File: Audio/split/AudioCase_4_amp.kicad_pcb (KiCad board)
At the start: 2 copper layers, 61.6 x 41.5 mm, 26 parts, among them J10 AMP_AUX_IN, J11 AMP_AUX_OUT, J9 AMP_PWR

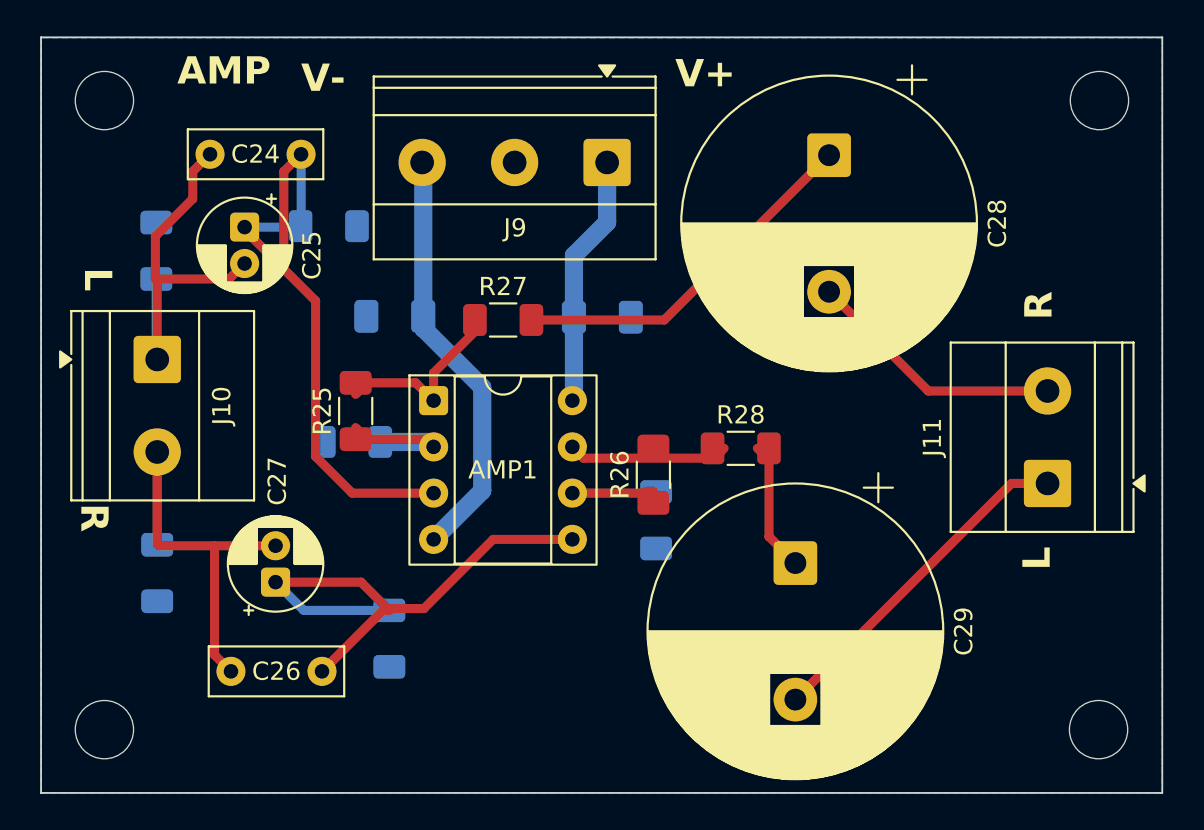
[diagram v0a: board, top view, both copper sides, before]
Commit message: ノイズ対策と製造データ整備: デカップリング追加・GNDベタ強化・シルク整理
- 5V_+ラインにデカップリング/バルク(C34-C37)を追加し、リレー切替時の電源変動を抑制
- F.CuにCTRL_GND/GNDベタを追加し、ステッチングビアで表裏GNDを補強(DC-DC周辺含む)
- 端子台ラベル等のシルク重なりを解消(J11/J14/J6/J4/L1/L2ほか)
- masterから4基板を再split、Gerber/zipを再生成

Co-authored-by: Cursor <cursoragent@cursor.com>
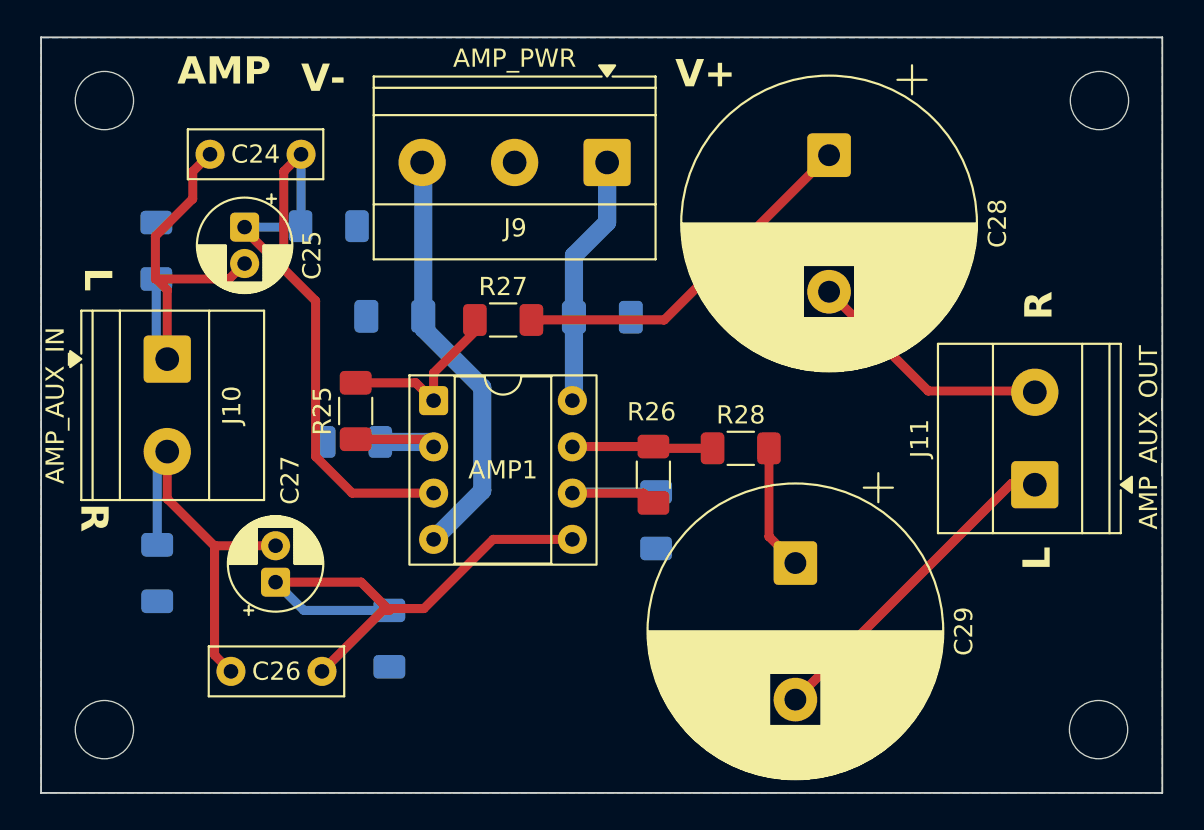
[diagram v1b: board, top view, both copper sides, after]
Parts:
- moved J11 0.70 mm to (172.3, 44.6)
- moved J10 0.55 mm to (124.6, 37.7)
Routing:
- net /Controll/L_OUT: track 24.0 -> 22.3 mm
- net Net-(AMP1-Pad7): track 8.82 -> 7.75 mm
- net Net-(AMP1A--): track 7.76 -> 6.86 mm
- net /Controll/R_OUT: track 22.2 -> 23.0 mm
- net /AmpModule/R_OUT: track 14.3 -> 13.6 mm
- net /AmpModule/L_OUT: track 18.8 -> 18.1 mm

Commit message: AudioCaseのリレー・EQネット整理と分割Gerberを再生成する。
Controllでアンプ別リレーネットを分離し、EQのバッファ入力をL/R_BUFF_INに改名。4枚分割PCBと発注用Gerberを更新し、RVパネルKiKit矩形とmacOS向けツール探索も修正。

Co-authored-by: Cursor <cursoragent@cursor.com>
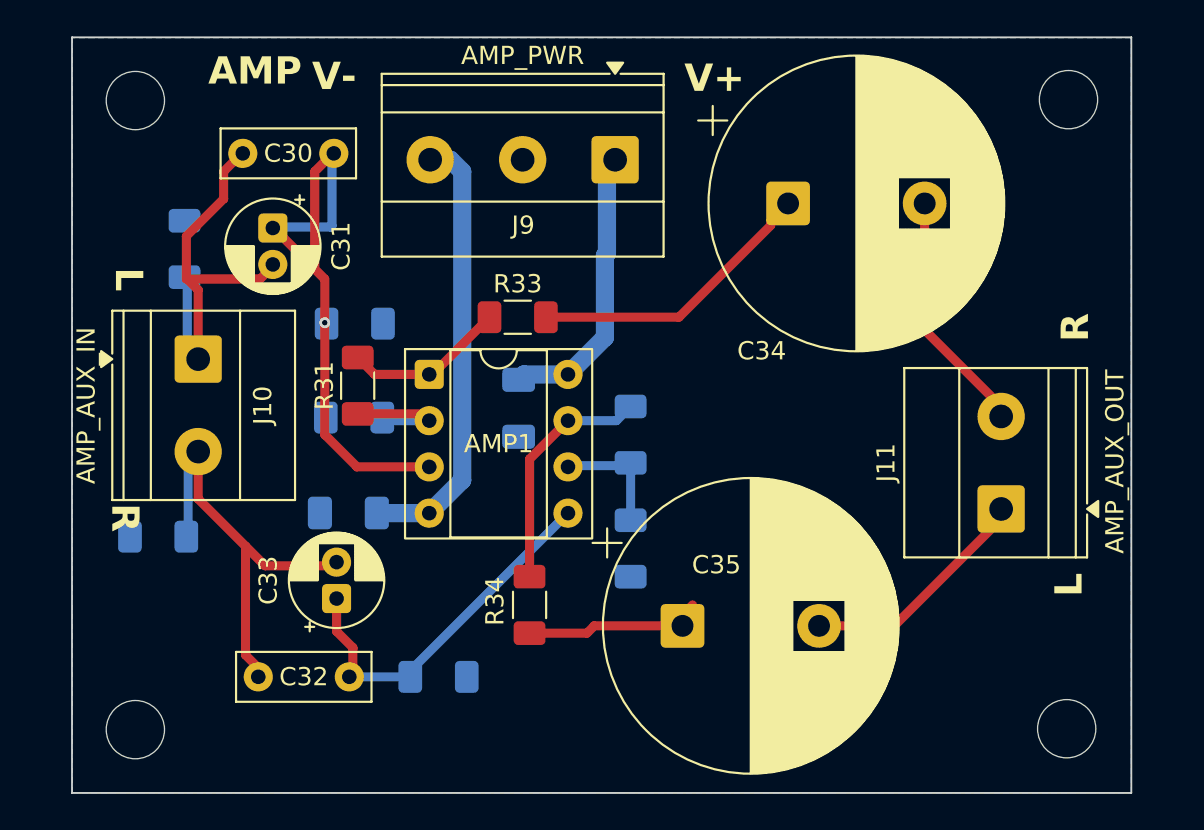
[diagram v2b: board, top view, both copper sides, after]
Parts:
- removed C22, C23: 0.1μF, Capacitor_SMD:C_1206_3216Metric_Pad1.33x1.80mm_HandSolder
- removed C24, C26: 0.1μF, Capacitor_THT:C_Rect_L7.2mm_W2.5mm_P5.00mm_FKS2_FKP2_MKS2_MKP2
- removed C25, C27: 10μF, Capacitor_THT:CP_Radial_D5.0mm_P2.00mm
- removed R19, R20: 220KΩ, Resistor_SMD:R_1206_3216Metric_Pad1.30x1.75mm_HandSolder
- removed R21, R22, R23, R24: 10KΩ, Resistor_SMD:R_1206_3216Metric_Pad1.30x1.75mm_HandSolder
- added C30: 0.1μF, Capacitor_THT:C_Rect_L7.2mm_W2.5mm_P5.00mm_FKS2_FKP2_MKS2_MKP2, F.Cu at (133.8, 26.4)
- added C31: 10μF, Capacitor_THT:CP_Radial_D5.0mm_P2.00mm, F.Cu at (130.4, 30.5)
- added C32: 0.1μF, Capacitor_THT:C_Rect_L7.2mm_W2.5mm_P5.00mm_FKS2_FKP2_MKS2_MKP2, F.Cu at (134.6, 55.1)
- added C33: 10μF, Capacitor_THT:CP_Radial_D5.0mm_P2.00mm, F.Cu at (133.9, 50.8)
- added C34: 470μF, Capacitor_THT:CP_Radial_D16.0mm_P7.50mm, F.Cu at (158.7, 29.1)
- added C35: 470μF, Capacitor_THT:CP_Radial_D16.0mm_P7.50mm, F.Cu at (152.9, 52.3)
- added R29: 10KΩ, Resistor_SMD:R_1206_3216Metric_Pad1.30x1.75mm_HandSolder, B.Cu at (134.9, 35.7)
- added R30: 10KΩ, Resistor_SMD:R_1206_3216Metric_Pad1.30x1.75mm_HandSolder, B.Cu at (150.1, 48.1)
- added R31: 47KΩ, Resistor_SMD:R_1206_3216Metric_Pad1.30x1.75mm_HandSolder, F.Cu at (135.1, 39.1)
- added R32: 47KΩ, Resistor_SMD:R_1206_3216Metric_Pad1.30x1.75mm_HandSolder, B.Cu at (150.1, 41.8)
- added R33: 47Ω, Resistor_SMD:R_1206_3216Metric_Pad1.30x1.75mm_HandSolder, F.Cu at (143.9, 35.4)
- added R34: 47Ω, Resistor_SMD:R_1206_3216Metric_Pad1.30x1.75mm_HandSolder, F.Cu at (144.5, 51.2)
- C28, C29: value 470μF -> 0.1μF; footprint Capacitor_THT:CP_Radial_D16.0mm_P7.50mm -> Capacitor_SMD:C_1206_3216Metric_Pad1.33x1.80mm_HandSolder; moved to B.Cu
- R25, R26: value 47KΩ -> 220KΩ; moved to B.Cu
- R27, R28: value 47Ω -> 10KΩ; moved to B.Cu
- moved R26 27.4 mm to (124.1, 47.4), turned to 180 degrees
- moved C29 24.7 mm to (134.6, 46.1), turned to 180 degrees
- moved C28 22.0 mm to (143.9, 40.4), turned to 90 degrees
- moved R28 20.8 mm to (139.5, 55.1), turned to 180 degrees
- moved R25 12.9 mm to (125.6, 31.6)
- moved R27 9.79 mm to (134.9, 40.9)
- moved J11 2.28 mm to (170.4, 45.9)
- moved H11 1.75 mm to (174.0, 58.0)
- moved H10 1.70 mm to (174.1, 23.4)
- moved H12 1.70 mm to (122.9, 58.0)
- moved H9 1.70 mm to (122.9, 23.5)
- moved J10 1.70 mm to (126.3, 37.7)
- moved AMP1 1.46 mm to (139.0, 38.5)
- moved J9 0.46 mm to (149.2, 26.7)
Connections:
- AMP1 pad 4: /Controll/AMP_V-_OUT -> /AmpModule/V-_IN
- AMP1 pad 8: /Controll/AMP_V+_OUT -> /AmpModule/V+_IN
- C28 pad 1: Net-(C28-Pad1) -> GND
- C28 pad 2: /AmpModule/R_OUT -> /AmpModule/V+_IN
- C29 pad 1: Net-(C29-Pad1) -> /AmpModule/V-_IN
- C29 pad 2: /AmpModule/L_OUT -> GND
- J10 pad 1: /Controll/R_OUT -> /AmpModule/R_IN
- J10 pad 2: /Controll/L_OUT -> /AmpModule/L_IN
- J9 pad 1: /Controll/AMP_V+_OUT -> /AmpModule/V+_IN
- J9 pad 3: /Controll/AMP_V-_OUT -> /AmpModule/V-_IN
- R25 pad 1: Net-(AMP1A--) -> /AmpModule/R_IN
- R25 pad 2: Net-(AMP1-Pad1) -> GND
- R26 pad 1: Net-(AMP1B--) -> /AmpModule/L_IN
- R26 pad 2: Net-(AMP1-Pad7) -> GND
- R27 pad 1: Net-(AMP1-Pad1) -> GND
- R27 pad 2: Net-(C28-Pad1) -> Net-(AMP1A--)
- R28 pad 1: Net-(AMP1-Pad7) -> GND
- R28 pad 2: Net-(C29-Pad1) -> Net-(AMP1B-+)
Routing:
- net /AmpModule/L_IN: track 0.00 -> 24.8 mm
- net /AmpModule/V-_IN: track 0.00 -> 24.4 mm
- net /Controll/AMP_V-_OUT: track 23.2 -> 0.00 mm
- net /AmpModule/R_IN: track 0.00 -> 23.0 mm
- net /Controll/R_OUT: track 23.0 -> 0.00 mm
- net /Controll/L_OUT: track 22.3 -> 0.00 mm
- net Net-(C28-Pad1): track 20.1 -> 0.00 mm
- net Net-(C34-Pad1): track 0.00 -> 16.0 mm
- net /AmpModule/V+_IN: track 0.00 -> 15.7 mm
- net Net-(AMP1B-+): track 35.7 -> 20.7 mm
- net /Controll/AMP_V+_OUT: track 13.9 -> 0.00 mm
- net Net-(C35-Pad1): track 0.00 -> 9.59 mm
- net Net-(C29-Pad1): track 6.90 -> 0.00 mm
- net Net-(AMP1-Pad7): track 7.75 -> 13.5 mm
- net /AmpModule/L_OUT: track 18.1 -> 13.5 mm
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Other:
- board size 61.6 x 41.5 mm -> 58.2 x 41.5 mm

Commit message: 分割Gerberを再生成し、05のzip名をスクリプト表記に揃える。
初号向け再出力を取り込み、旧05_rv_conv.zipを05_rv_convert.zipへ置き換える。

Co-authored-by: Cursor <cursoragent@cursor.com>
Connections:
- net /AmpModule/L_OUT renamed /MeasurementADC/AUDIO_L_IN
- net /AmpModule/R_OUT renamed /MeasurementADC/AUDIO_R_IN
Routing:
- net /MeasurementADC/AUDIO_L_IN: track 13.5 -> 12.7 mm
